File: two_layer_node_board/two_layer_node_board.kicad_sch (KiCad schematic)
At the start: 5 parts, among them J1 Screw_Terminal_01x04, U1 THVD1450D

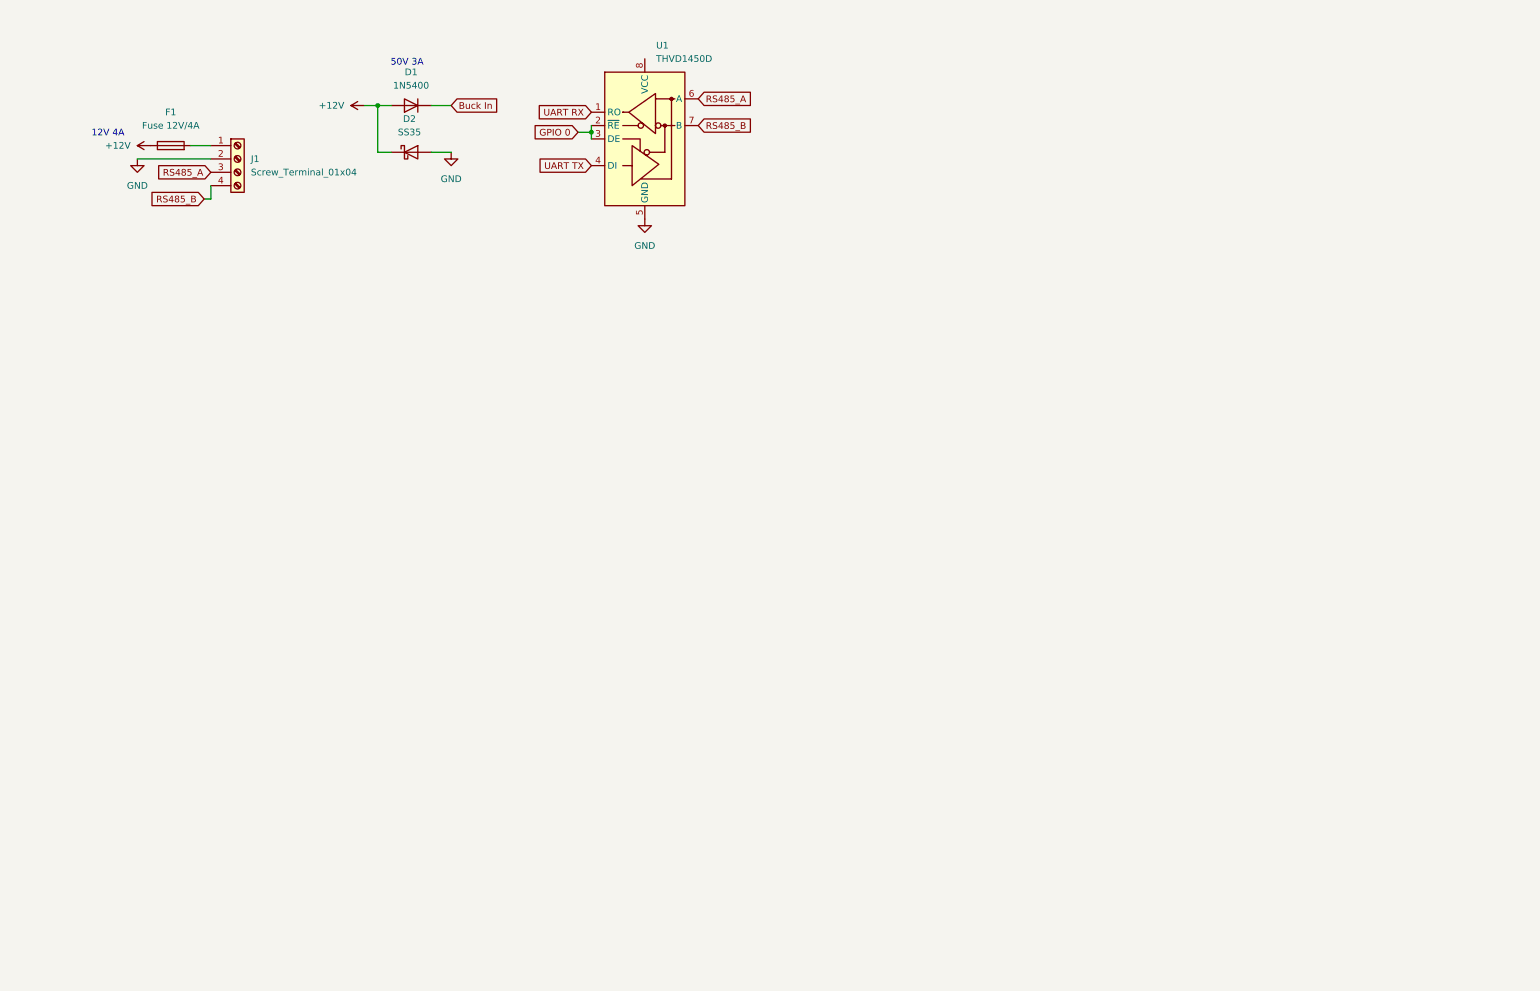
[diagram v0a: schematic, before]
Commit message: More schematic progress on node board
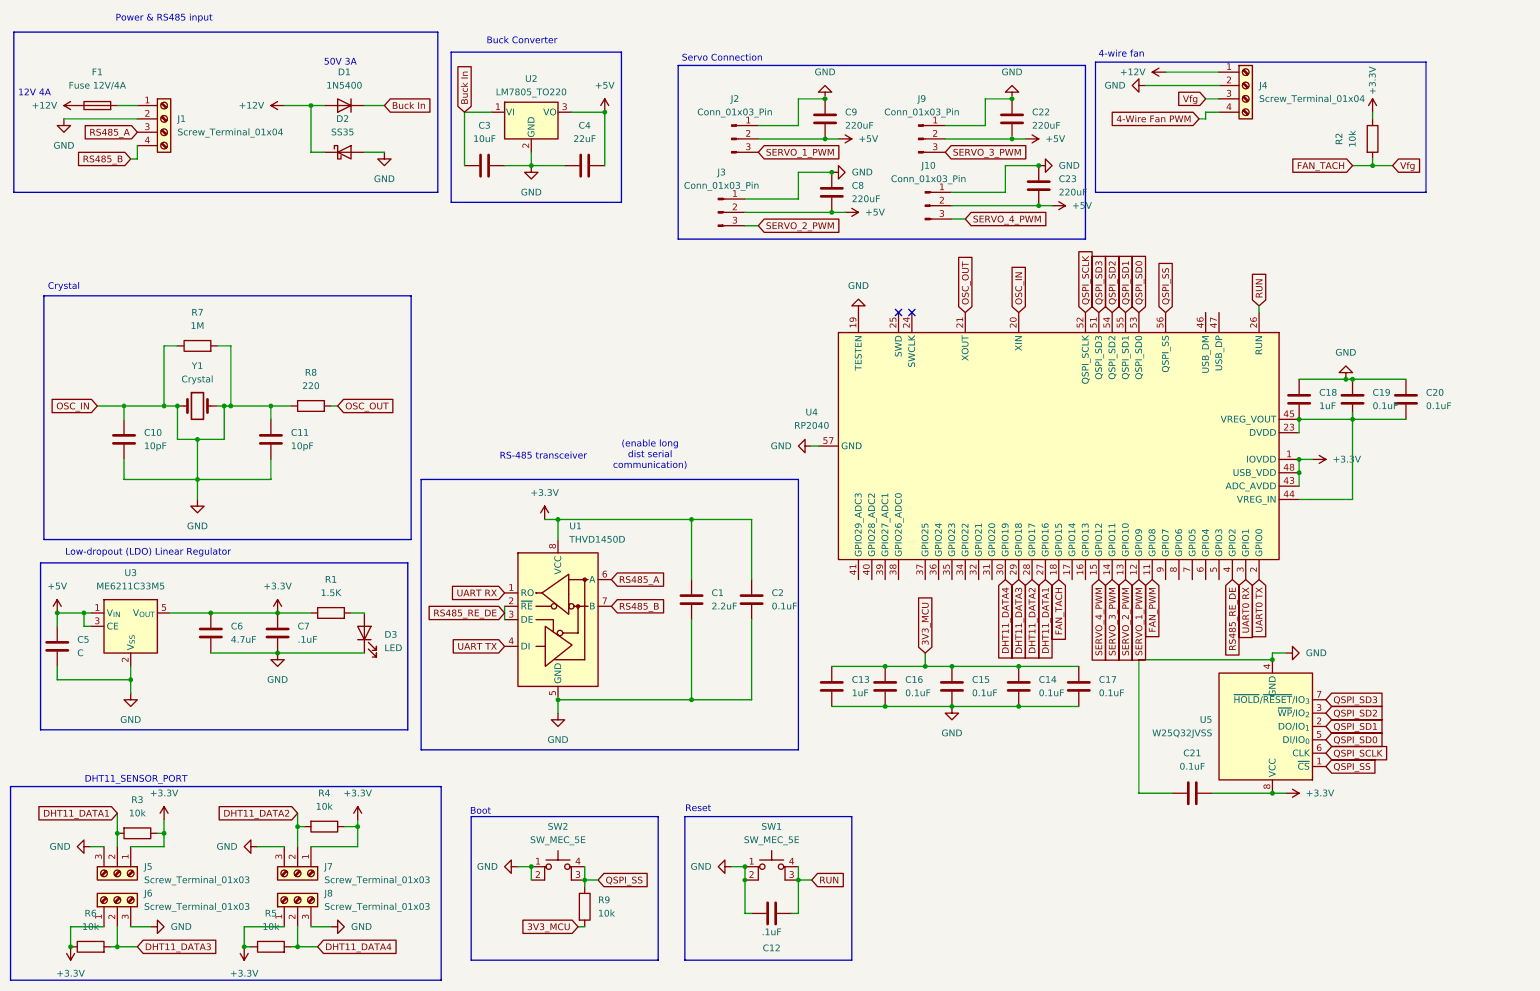
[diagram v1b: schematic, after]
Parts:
- added C1: 2.2uF, Connector_PinSocket_2.54mm:PinSocket_1x04_P2.54mm_Vertical, symbol Device:C
- added C10, C11: 10pF, symbol Device:C
- added C12, C7: .1uF, symbol Device:C
- added C13, C18: 1uF, symbol Device:C
- added C14, C15, C16, C17, C19, C2, C20, C21: 0.1uF, symbol Device:C
- added C22, C23, C8, C9: 220uF, symbol Device:C
- added C3: 10uF, symbol Device:C
- added C4: 22uF, symbol Device:C
- added C5: C, symbol Device:C
- added C6: 4.7uF, symbol Device:C
- added D3: LED, symbol Device:LED
- added J10, J2, J3, J9: Conn_01x03_Pin, Connector_PinHeader_2.54mm:PinHeader_1x03_P2.54mm_Vertical, symbol Connector:Conn_01x03_Pin
- added J4: Screw_Terminal_01x04, symbol Connector:Screw_Terminal_01x04
- added J5, J6, J7, J8: Screw_Terminal_01x03, symbol Connector:Screw_Terminal_01x03
- added R1: 1.5K, symbol Device:R
- added R2, R3, R4, R5, R6, R9: 10k, symbol Device:R
- added R7: 1M, symbol Device:R
- added R8: 220, symbol Device:R
- added SW1, SW2: SW_MEC_5E, symbol Switch:SW_MEC_5E
- added U2: LM7805_TO220, Package_TO_SOT_THT:TO-220-3_Vertical, symbol Regulator_Linear:LM7805_TO220
- added U3: ME6211C33M5, Package_TO_SOT_SMD:SOT-23-5, symbol Regulator_Linear:ME6211C33M5
- added U4: RP2040, Package_DFN_QFN:QFN-56-1EP_7x7mm_P0.4mm_EP3.2x3.2mm, symbol MCU_RaspberryPi:RP2040
- added U5: W25Q32JVSS, Package_SO:SOIC-8_5.3x5.3mm_P1.27mm, symbol Memory_Flash:W25Q32JVSS
- added Y1: Crystal, symbol Device:Crystal
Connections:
- net +12V: now also J4.1 (Pin_1)
- net Buck In: now also C3.1, U2.1 (VI)
- net GND: now also C1.2, C10.1, C10.2, C11.1, C11.2, C12.1, C13.2, C14.2, C15.2, C16.2, C17.2, C18.1, C19.1, C2.2, C20.1, C21.1, C22.1, C23.2, C3.2, C4.2, C5.2, C6.2, C7.2, C8.2, C9.1, D3.1 (K), J10.1 (Pin_1), J2.1 (Pin_1), J3.1 (Pin_1), J4.2 (Pin_2), J5.3 (Pin_3), J6.3 (Pin_3), J7.3 (Pin_3), J8.3 (Pin_3), J9.1 (Pin_1), R7.1, R7.2, R8.1, SW1.1, SW1.2, SW2.1, SW2.2, U2.2 (GND), U3.2 (V_{SS}), U4.19 (TESTEN), U4.20 (XIN), U4.57 (GND), U5.4 (GND), Y1.1, Y1.2
- net +3.3V: now reaches U1.8 (VCC)
- net +3.3V: now also C1.1, C2.1, C21.2, C6.1, C7.1, J5.1 (Pin_1), J6.1 (Pin_1), J7.1 (Pin_1), J8.1 (Pin_1), R1.1, R2.1, R3.1, R4.1, R5.1, R6.1, U3.5 (V_{OUT}), U4.1 (IOVDD), U4.10 (IOVDD), U4.22 (IOVDD), U4.33 (IOVDD), U4.42 (IOVDD), U4.43 (ADC_AVDD), U4.48 (USB_VDD), U4.49 (IOVDD), U5.8 (VCC)
- net GPIO 0 renamed RS485_RE_DE
- net RS485_RE_DE: now also U4.4 (GPIO2)
- new net: C18.2, C19.2, C20.2, U4.23 (DVDD), U4.44 (VREG_IN), U4.45 (VREG_VOUT), U4.50 (DVDD)
- new net: D3.2 (A), R1.2
- new net +5V: C22.2, C23.1, C4.1, C5.1, C8.1, C9.2, J10.2 (Pin_2), J2.2 (Pin_2), J3.2 (Pin_2), J9.2 (Pin_2), U2.3 (VO), U3.1 (V_{IN}), U3.3 (CE)
- new net 3V3_MCU: C13.1, C14.1, C15.1, C16.1, C17.1, R9.2
- new net 4-Wire Fan PWM: J4.4 (Pin_4)
- new net DHT11_DATA1: J5.2 (Pin_2), R3.2, U4.27 (GPIO16)
- new net DHT11_DATA2: J7.2 (Pin_2), R4.2, U4.28 (GPIO17)
- new net DHT11_DATA3: J6.2 (Pin_2), R6.2, U4.29 (GPIO18)
- new net DHT11_DATA4: J8.2 (Pin_2), R5.2, U4.30 (GPIO19)
- new net FAN_PWM: U4.11 (GPIO8)
- new net FAN_TACH: J4.3 (Pin_3), R2.2, U4.18 (GPIO15)
- new net OSC_OUT: R8.2, U4.21 (XOUT)
- new net QSPI_SCLK: U4.52 (QSPI_SCLK), U5.6 (CLK)
- new net QSPI_SD0: U4.53 (QSPI_SD0), U5.5 (DI/IO_{0})
- new net QSPI_SD1: U4.55 (QSPI_SD1), U5.2 (DO/IO_{1})
- new net QSPI_SD2: U4.54 (QSPI_SD2), U5.3 (~{WP}/IO_{2})
- new net QSPI_SD3: U4.51 (QSPI_SD3), U5.7 (~{HOLD}/~{RESET}/IO_{3})
- new net QSPI_SS: R9.1, SW2.3 (K), SW2.4 (A), U4.56 (QSPI_SS), U5.1 (~{CS})
- new net RUN: C12.2, SW1.3 (K), SW1.4 (A), U4.26 (RUN)
- new net SERVO_1_PWM: J2.3 (Pin_3), U4.12 (GPIO9)
- new net SERVO_2_PWM: J3.3 (Pin_3), U4.13 (GPIO10)
- new net SERVO_3_PWM: J9.3 (Pin_3), U4.14 (GPIO11)
- new net SERVO_4_PWM: J10.3 (Pin_3), U4.15 (GPIO12)
- new net UART0 RX: U4.3 (GPIO1)
- new net UART0 TX: U4.2 (GPIO0)
- no-connect marks 0 -> 2
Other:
- note added: "(enable long dist serial communication)"
- note added: "4-wire fan"
- note added: "Boot"
- note added: "Buck Converter"
- note added: "Crystal"
- note added: "DHT11_SENSOR_PORT"
- note added: "Low-dropout (LDO) Linear Regulator"
- note added: "Power & RS485 input"
- note added: "RS-485 transceiver"
- note added: "Reset"
- note added: "Servo Connection"
- moved on the sheet: D1, D2, F1, J1, U1

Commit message: Added a schematic for the controller board
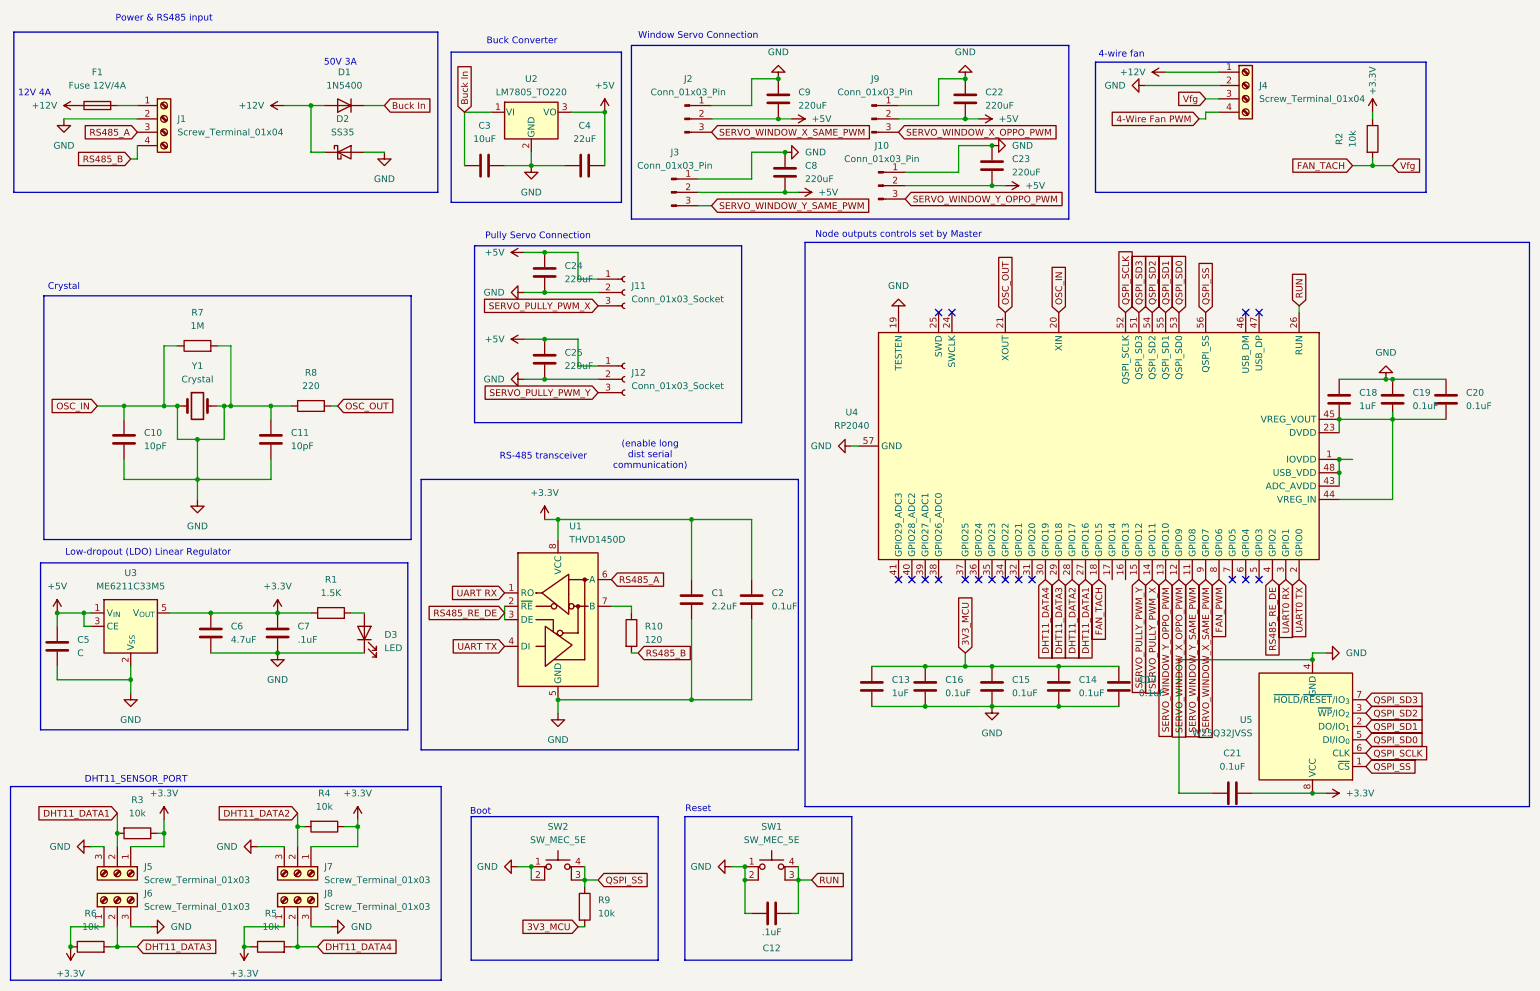
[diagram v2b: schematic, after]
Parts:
- added C24, C25: 220uF, symbol Device:C
- added J11, J12: Conn_01x03_Socket, symbol Connector:Conn_01x03_Socket
- added R10: 120, symbol Device:R
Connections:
- net +3.3V: no longer U4.1 (IOVDD), U4.10 (IOVDD), U4.22 (IOVDD), U4.33 (IOVDD), U4.42 (IOVDD), U4.43 (ADC_AVDD), U4.48 (USB_VDD), U4.49 (IOVDD)
- net +5V: now also C24.1, C25.1, J11.1 (Pin_1), J12.1 (Pin_1)
- net FAN_PWM: now also U4.8 (GPIO6); no longer U4.11 (GPIO8)
- net GND: now also C24.2, C25.2, J11.2 (Pin_2), J12.2 (Pin_2)
- net RS485_B: now also R10.2; no longer U1.7 (B)
- net SERVO_WINDOW_X_SAME_PWM: now reaches U4.9 (GPIO7)
- net SERVO_WINDOW_X_SAME_PWM: now also J2.3 (Pin_3)
- net SERVO_1_PWM renamed SERVO_WINDOW_X_OPPO_PWM
- net SERVO_WINDOW_X_OPPO_PWM: now also J9.3 (Pin_3); no longer J2.3 (Pin_3)
- net SERVO_2_PWM renamed SERVO_WINDOW_Y_OPPO_PWM
- net SERVO_WINDOW_Y_OPPO_PWM: now also J10.3 (Pin_3); no longer J3.3 (Pin_3)
- net SERVO_3_PWM renamed SERVO_PULLY_PWM_X
- net SERVO_PULLY_PWM_X: now also J11.3 (Pin_3); no longer J9.3 (Pin_3)
- net SERVO_4_PWM renamed SERVO_PULLY_PWM_Y
- net SERVO_PULLY_PWM_Y: now also J12.3 (Pin_3); no longer J10.3 (Pin_3)
- new net: U4.1 (IOVDD), U4.10 (IOVDD), U4.22 (IOVDD), U4.33 (IOVDD), U4.42 (IOVDD), U4.43 (ADC_AVDD), U4.48 (USB_VDD), U4.49 (IOVDD)
- new net: R10.1, U1.7 (B)
- new net SERVO_WINDOW_Y_SAME_PWM: J3.3 (Pin_3), U4.11 (GPIO8)
- no-connect marks 2 -> 17
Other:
- note added: "Node outputs controls set by Master"
- note added: "Pully Servo Connection"
- note added: "Window Servo Connection"
- note removed: "Servo Connection"
- moved on the sheet: C13, C14, C15, C16, C17, C18, C19, C20, C21, C22, C23, C8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
